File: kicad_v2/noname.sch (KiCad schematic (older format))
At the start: 13 parts

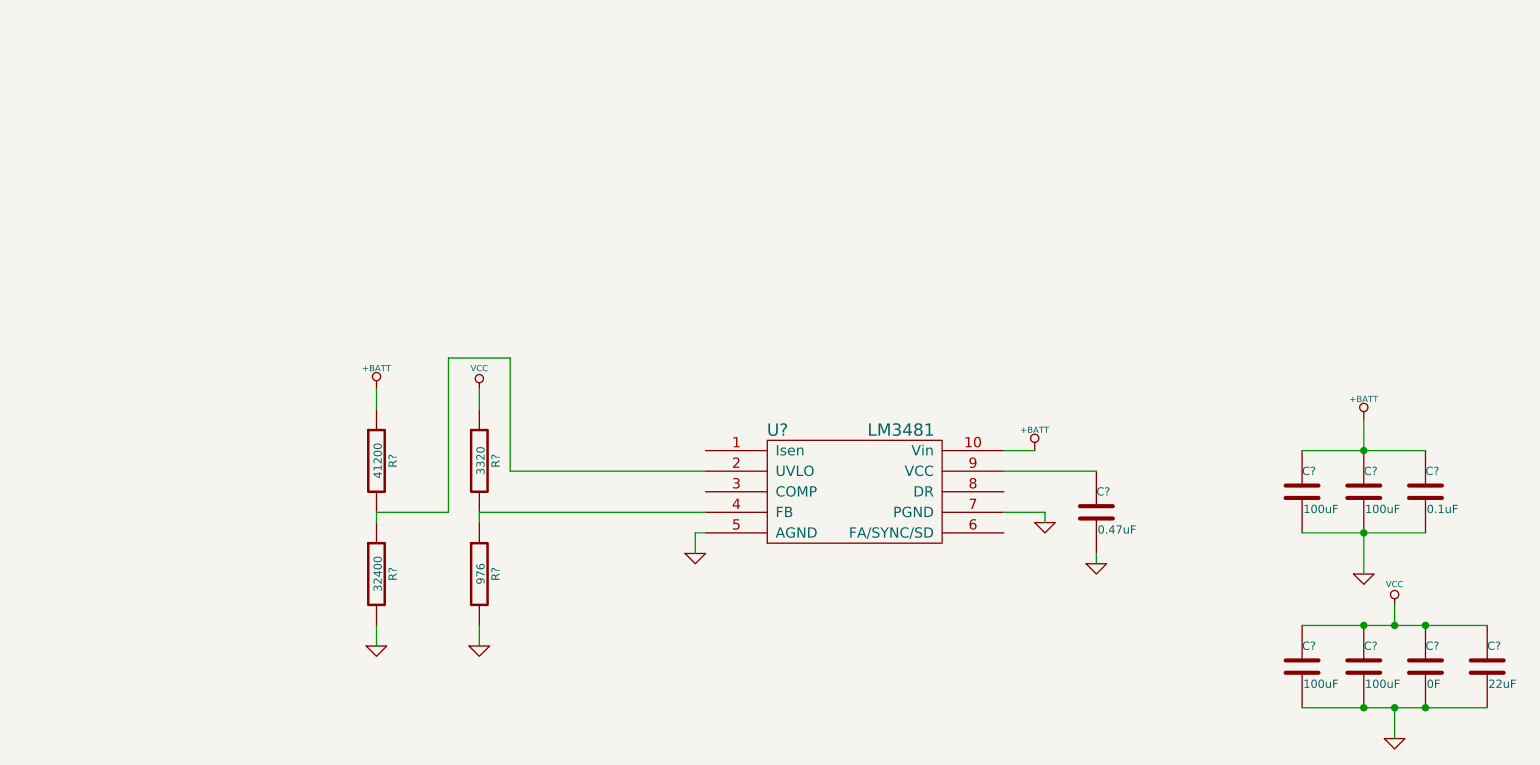
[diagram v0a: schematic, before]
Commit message: upgraded to kicad r4885 and almost finished revised powerboard schematic
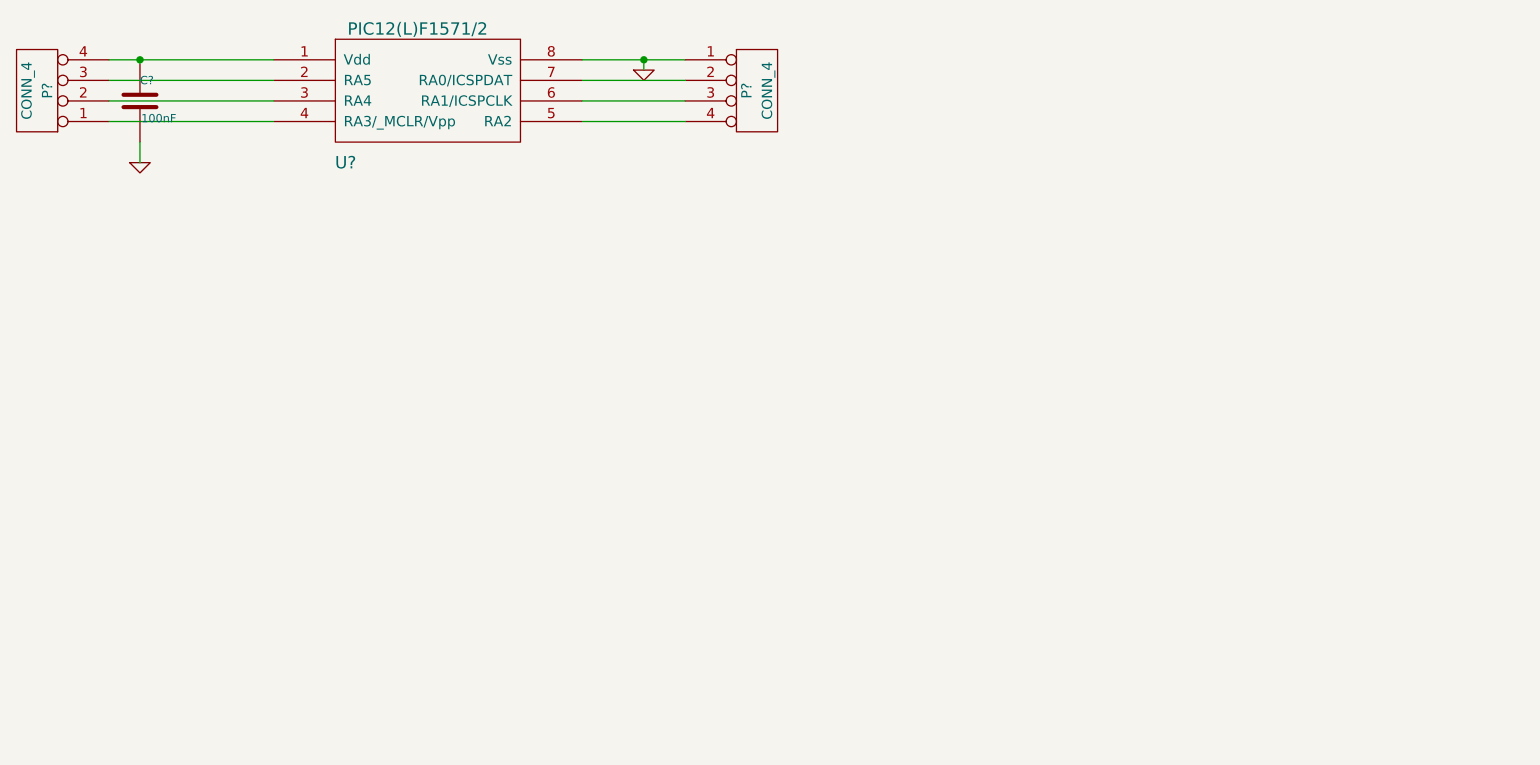
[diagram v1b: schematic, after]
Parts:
- removed C? (x4): 100uF, symbol C
- removed C?: 0.1uF, symbol C
- removed C?: 0F, symbol C
- removed C?: 22uF, symbol C
- removed C?: 0.47uF, symbol C
- removed R?: 3320, symbol R
- removed R?: 976, symbol R
- removed R?: 41200, symbol R
- removed R?: 32400, symbol R
- removed U?: LM3481, symbol LM3481
- added C?: 100nF, symbol C
- added P? (x2): CONN_4, symbol CONN_4
- added U?: PIC12(L)F1571/2, symbol PIC12(L)F1571/2
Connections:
- net GND: now also C?.2, P?.1 (P1), U?.8 (Vss)
- new net: C?.1, P?.4 (P4), U?.1 (Vdd)
- new net: P?.3 (P3), U?.2 (RA5)
- new net: P?.2 (P2), U?.3 (RA4)
- new net: P?.1 (P1), U?.4 (RA3/_MCLR/Vpp)
- new net: P?.4 (P4), U?.5 (RA2)
- new net: P?.3 (P3), U?.6 (RA1/ICSPCLK)
- new net: P?.2 (P2), U?.7 (RA0/ICSPDAT)
